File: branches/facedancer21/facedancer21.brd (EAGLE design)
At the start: 71.1 x 23.5 mm, 20 parts, among them CN1 HOST, CN2 TARGET, CN3 USB-A-S, Q1 12MHz, U1 F261X---PM64, U2 FT232RL-BASICSSOP, U4 MAX3421ESMD

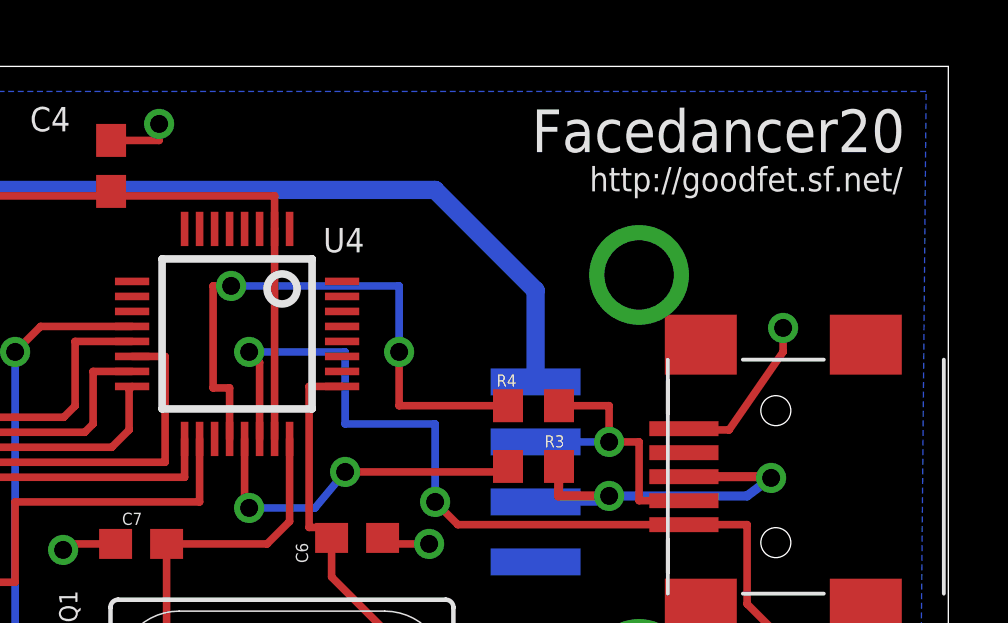
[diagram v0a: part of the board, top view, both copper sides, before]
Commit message: FD21 fixing FD20 errata.
git-svn-id: https://svn.code.sf.net/p/goodfet/code@1378 12e2690d-a6be-4b82-a7b7-67c4a43b65c8
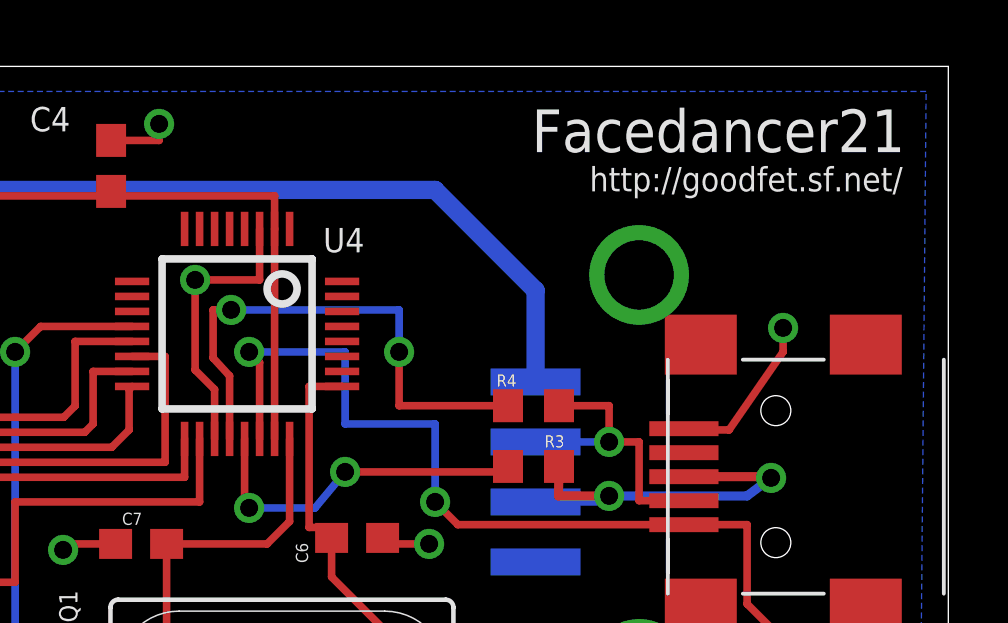
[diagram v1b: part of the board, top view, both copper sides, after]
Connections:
- net GND: now also U4.19, U4.3
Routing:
- net GND: track 45.3 -> 54.7 mm, vias 10 -> 11
- net DMINUS: track 19.5 -> 17.6 mm
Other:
- board text added: "Facedancer21"
- board text removed: "Facedancer20"
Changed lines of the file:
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@@
 <text x="30.7975" y="7.62" size="0.4064" layer="25" rot="R90">RXD</text>
 <text x="29.21" y="4.445" size="0.4064" layer="25" rot="R90">TXD</text>
-<text x="69.66" y="22.0825" size="1.4224" layer="25" font="vector" rot="R180">Facedancer20</text>
+<text x="69.66" y="22.0825" size="1.4224" layer="25" font="vector" rot="R180">Facedancer21</text>
 <text x="1.07" y="21.905" size="1.2192" layer="25" font="vector">TravisGoodspeed&lt;travis@tnbelt.com&gt;</text>
 <text x="1.07" y="20" size="1.4224" layer="25" font="vector">+1.865.471.8519</text>
@@
 <wire x1="18.785" y1="6.1865" x2="18.785" y2="7.35" width="0.254" layer="1"/>
 <wire x1="18.785" y1="7.35" x2="19.435" y2="8" width="0.254" layer="1"/>
+<contactref element="U4" pad="3"/>
+<contactref element="U4" pad="19"/>
+<wire x1="46.65" y1="11.1" x2="46.65" y2="12.75" width="0.254" layer="1"/>
+<wire x1="46.65" y1="12.75" x2="46" y2="13.4" width="0.254" layer="1"/>
+<wire x1="46" y1="13.4" x2="46" y2="16.4" width="0.254" layer="1"/>
+<wire x1="46" y1="16.4" x2="48.15" y2="16.4" width="0.254" layer="1"/>
+<wire x1="48.15" y1="18.1" x2="48.15" y2="16.4" width="0.254" layer="1"/>
+<via x="46" y="16.4" extent="1-16" drill="0.6"/>
 </signal>
 <signal name="N$1">
@@
 <contactref element="U4" pad="20"/>
 <contactref element="R4" pad="1"/>
-<via x="47.2" y="16.2" extent="1-16" drill="0.6" shape="square"/>
-<wire x1="47.2" y1="16.2" x2="52.8" y2="16.2" width="0.254" layer="16"/>
-<wire x1="52.8" y1="16.2" x2="52.8" y2="14" width="0.254" layer="16"/>
+<via x="47.2" y="15.4" extent="1-16" drill="0.6"/>
+<wire x1="47.2" y1="15.4" x2="52.8" y2="15.4" width="0.254" layer="16"/>
+<wire x1="52.8" y1="15.4" x2="52.8" y2="14" width="0.254" layer="16"/>
 <via x="52.8" y="14" extent="1-16" drill="0.6" shape="square"/>
 <wire x1="52.8" y1="14" x2="52.83" y2="14" width="0.254" layer="1"/>
-<wire x1="47.15" y1="11.1" x2="47.15" y2="12.8" width="0.254" layer="1"/>
-<wire x1="47.15" y1="12.8" x2="46.6" y2="12.8" width="0.254" layer="1"/>
-<wire x1="46.6" y1="12.8" x2="46.6" y2="16.2" width="0.254" layer="1"/>
-<wire x1="46.6" y1="16.2" x2="47.2" y2="16.2" width="0.254" layer="1"/>
+<wire x1="47.15" y1="11.1" x2="47.15" y2="13.2" width="0.254" layer="1"/>
+<wire x1="47.15" y1="13.2" x2="46.6" y2="13.8" width="0.254" layer="1"/>
+<wire x1="46.6" y1="13.8" x2="46.6" y2="15.4" width="0.254" layer="1"/>
+<wire x1="46.6" y1="15.4" x2="47.2" y2="15.4" width="0.254" layer="1"/>
 <wire x1="56.43" y1="12.2075" x2="52.8" y2="12.2075" width="0.254" layer="1"/>
 <wire x1="52.8" y1="12.2075" x2="52.8" y2="14" width="0.254" layer="1"/>
